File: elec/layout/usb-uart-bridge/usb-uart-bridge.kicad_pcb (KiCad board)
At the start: 2 copper layers, 8 parts

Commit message: Build everything with ordered params to fix frozen builds
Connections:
- C1 pad 1: hv-1 -> hv-2
- C2 pad 1: hv-1 -> hv-2
- C3 pad 1: hv-2 -> hv
- C4 pad 1: hv-2 -> hv
- D1 pad 4: hv -> hv-1
- R2 pad 2: hv-2 -> hv
- U1 pad 6: hv-2 -> hv
- U1 pad 7: hv-1 -> hv-2
- U1 pad 8: hv -> hv-1
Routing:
- net hv-1: track 3.36 -> 8.66 mm, vias 0 -> 2
- net hv-2: track 6.20 -> 3.36 mm, vias 2 -> 0
- net hv: track 8.66 -> 6.20 mm

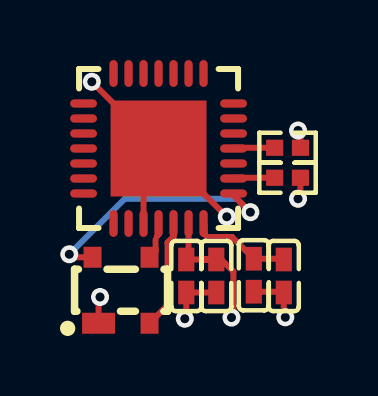
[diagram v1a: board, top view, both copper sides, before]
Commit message: Cleanup layout for usb hub and usb-uart, add CM5 controller heatsink outline
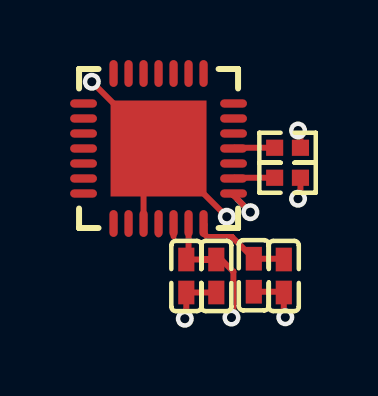
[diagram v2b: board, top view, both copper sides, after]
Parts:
- removed D1: , atopile:SOT-143_L2.9-W1.3-P1.92-LS2.3-BR-44397f
- C4: value 4.7µF ±20% 6.3V X5R -> 4.7µF ±20% 10V X5R
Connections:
- C1 pad 1: hv-2 -> hv-1
- C2 pad 1: hv-2 -> hv-1
- U1 pad 7: hv-2 -> hv-1
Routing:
- net hv-1: track 8.66 -> 4.85 mm, vias 2 -> 1
- net hv-2: track 3.36 -> 0.00 mm
- net Dminus: track 3.66 -> 0.43 mm
- net gnd: track 14.3 -> 13.4 mm, vias 6 -> 5
- net Dplus: track 1.13 -> 0.37 mm
